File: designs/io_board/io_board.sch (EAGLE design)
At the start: 47 parts, among them U6 MSP430FR5739IDA

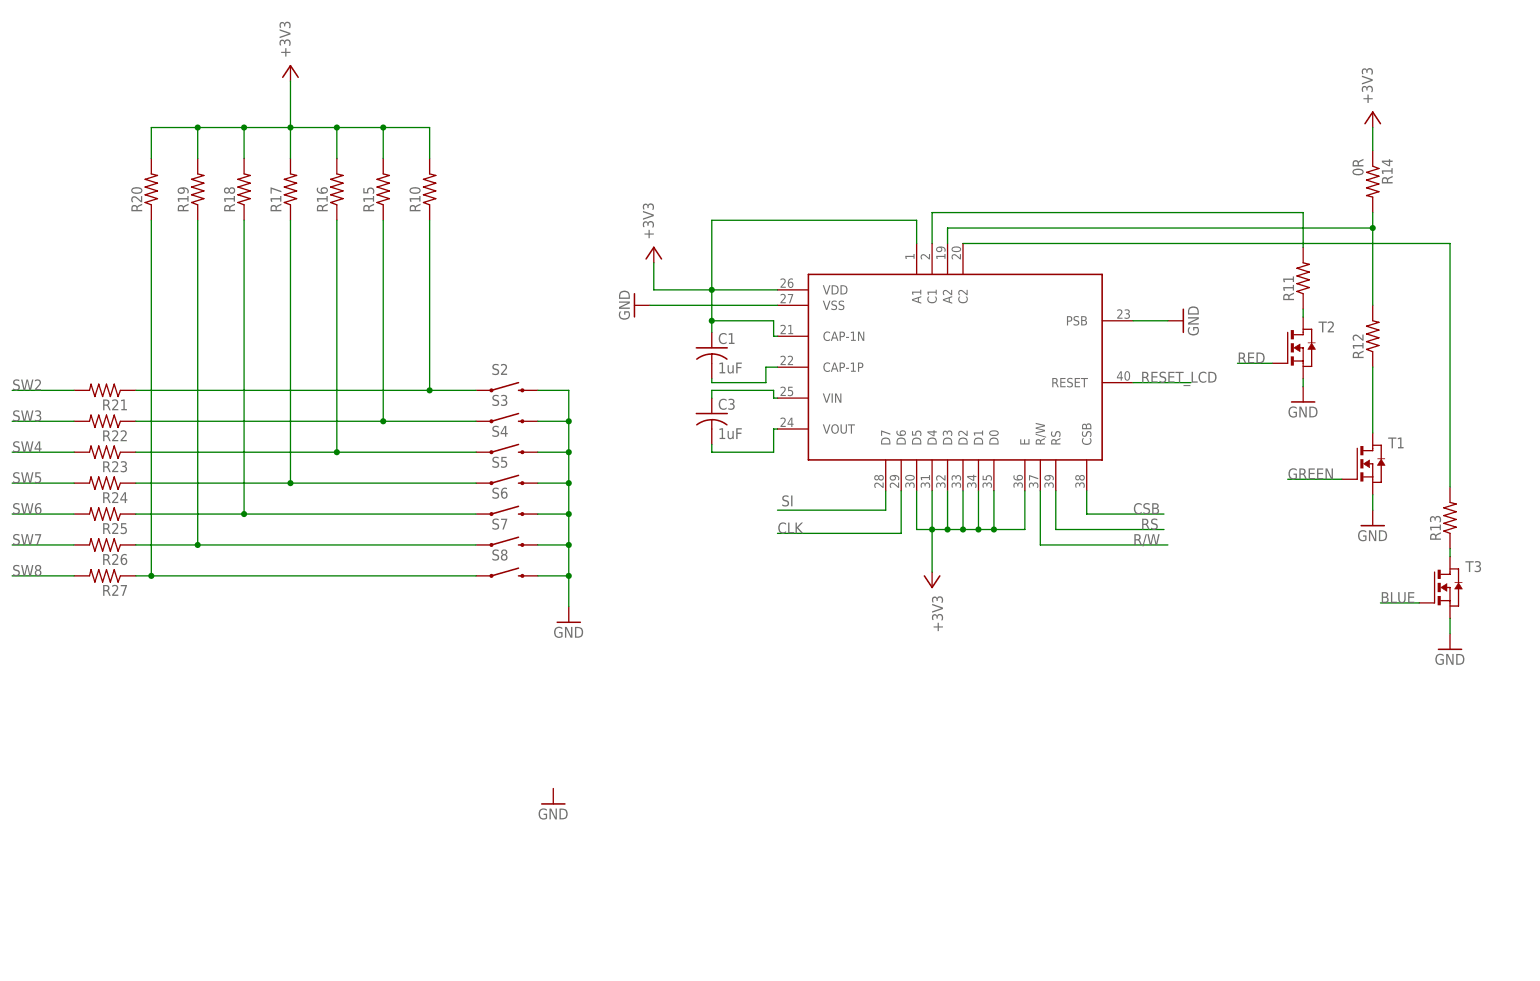
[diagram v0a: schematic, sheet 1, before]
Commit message: Adding bord file for lcd screen
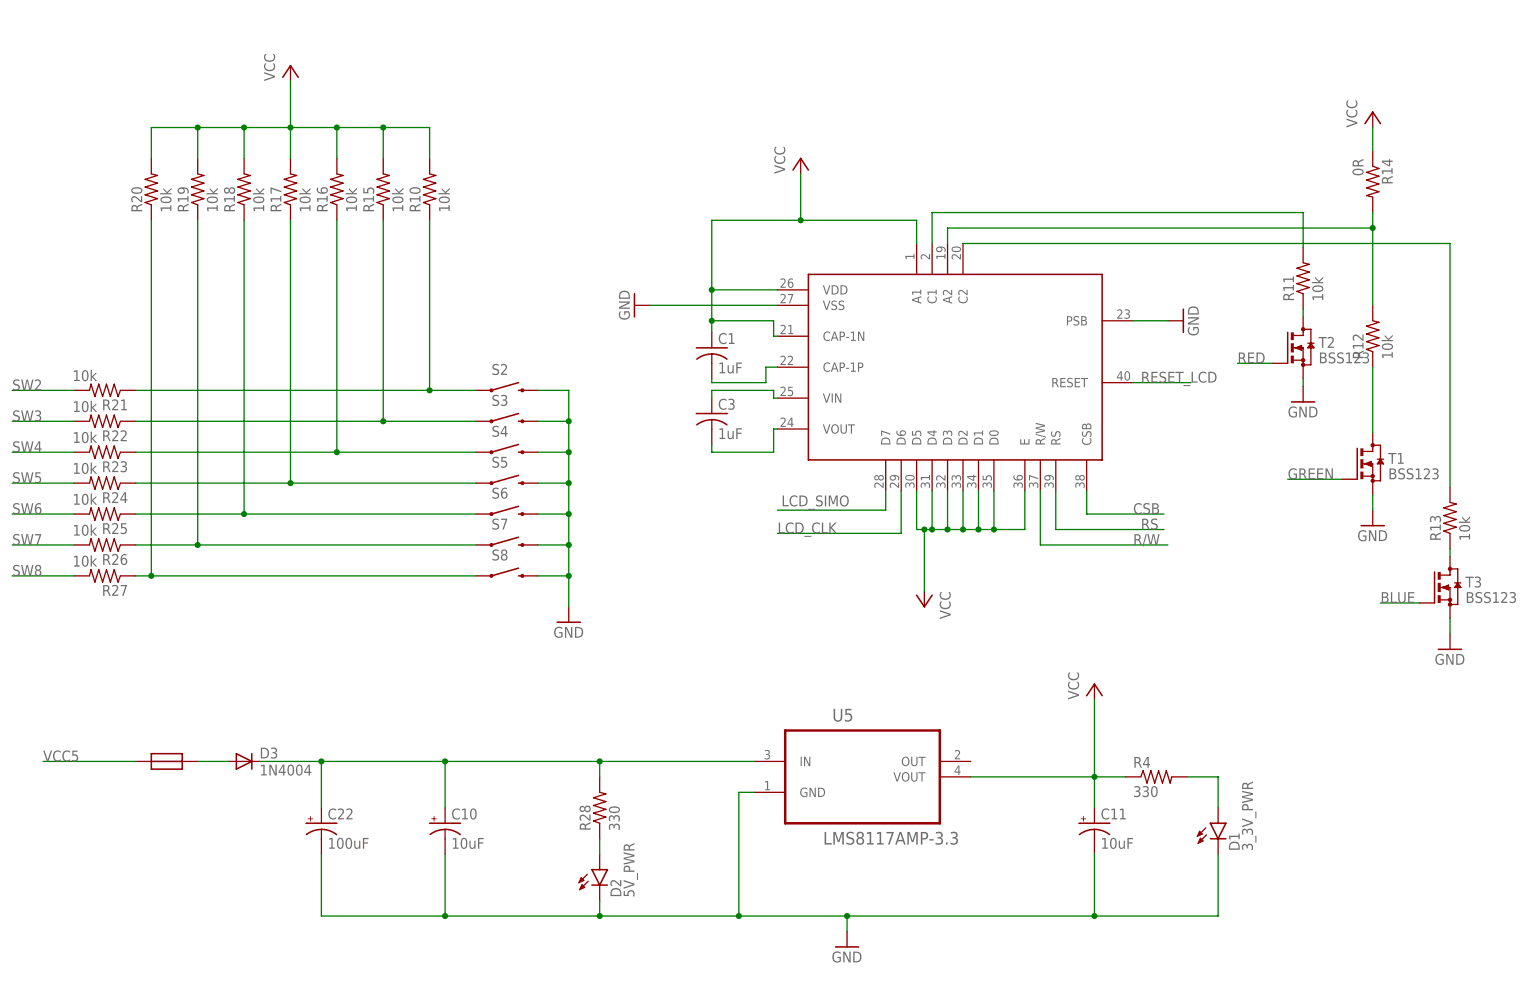
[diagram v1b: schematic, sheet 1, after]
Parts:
- added C10, C11: 10uF, SparkFun-Capacitors:10UF-16V-10%(TANT)
- added C22: 100uF, SparkFun-Capacitors:100UF-10V-10%(TANT)
- added D1: 3_3V_PWR, SparkFun-LED:LED-FKIT-1206
- added D2: 5V_PWR, SparkFun-LED:LED-FKIT-1206
- added D3: 1N4004, diode:1N4004
- added J1: 22-05-7068-06, con-molex:22-05-7068-06
- added R28, R4: 330, rcl:R-US_R0805W
- added R29, R30: 4.7k, rcl:R-US_R0805W
- added U$3: NANO_FUSE, custom_fuses:NANO_FUSE
- added U5: LMS8117AMP-3.3, NSC-LMS8117AMP:LMS8117AMP-3.3
- R10, R11, R12, R13, R15, R16, R17, R18, R19, R20, R21, R22, R23, R24, R25, R26, R27: value (none) -> 10k
- T1, T2, T3: value (none) -> BSS123; device zetex:NMOSSOT223 -> transistor-small-signal:BSS123
- renumbered JP1 to JTAG
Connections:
- removed net +3V3: C1.1, R10.2, R14.1, R15.2, R16.2, R17.2, R18.2, R19.2, R20.2, U$2.A1, U$2.CAP-1N, U$2.D0, U$2.D1, U$2.D2, U$2.D3, U$2.D4, U$2.D5, U$2.E, U$2.VDD
- removed net 3.3V: C14.1, C15.1, R6.2, R7.2, R9.2, U6.AVCC, U6.DVCC
- removed net CLK: U$2.D6
- removed net MISO: U6.P2.6
- removed net MOSI: U6.P2.5
- removed net SI: U$2.D7
- new net LCD_CLK: U$2.D6, U6.P2.4
- new net LCD_SIMO: U$2.D7, U6.P2.5
- new net N$23: D1.A, R4.2
- new net N$24: D2.A, R28.1
- new net N$25: D3.A, U$3.2
- new net N$27: C10.+, C22.+, D3.C, R28.2, U5.IN
- new net SIMO_SDA: J1-4.S, R30.1, U6.P1.6
- new net SOMI_SCL: J1-3.S, R29.1, U6.P1.7
- new net SPI_CLK: J1-5.S, U6.P2.2
- new net SPI_EN: J1-6.S, U6.P1.3
- new net VCC: C1.1, C11.+, C14.1, C15.1, R10.2, R14.1, R15.2, R16.2, R17.2, R18.2, R19.2, R20.2, R29.2, R30.2, R4.1, R6.2, R7.2, R9.2, U$2.A1, U$2.CAP-1N, U$2.D0, U$2.D1, U$2.D2, U$2.D3, U$2.D4, U$2.D5, U$2.E, U$2.VDD, U5.VOUT, U6.AVCC, U6.DVCC
- new net VCC5: J1-2.S, U$3.1
- net BLUE: now also U6.P2.0
- net CSB: now also U6.P2.3
- net GND: now also C10.-, C11.-, C22.-, D1.C, D2.C, J1-1.S, U5.GND
- net GREEN: now also U6.P3.4
- net R/W: now also U6.P3.5
- net RED: now also U6.P1.4
- net RESET_LCD: now also U6.P2.1
